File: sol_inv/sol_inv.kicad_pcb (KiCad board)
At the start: 2 copper layers, 0 parts

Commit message: initial component placement
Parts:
- added C1: 1nF, Capacitor_SMD:C_0603_1608Metric, F.Cu at (217.0, 65.0)
- added C10: 10uF, Capacitor_SMD:C_0603_1608Metric, F.Cu at (183.5, 83.5)
- added C11: 10uF, Capacitor_SMD:C_0603_1608Metric, F.Cu at (183.5, 104.5)
- added C12: 10uF, Capacitor_SMD:C_0603_1608Metric, F.Cu at (188.5, 83.3)
- added C13: 0.1uF, Capacitor_SMD:C_0201_0603Metric, F.Cu at (179.3, 92.5)
- added C14: 0.1uF, Capacitor_SMD:C_0201_0603Metric, F.Cu at (184.0, 86.0)
- added C15: 0.1uF, Capacitor_SMD:C_0201_0603Metric, F.Cu at (189.0, 86.0)
- added C16: 0.1uF, Capacitor_SMD:C_0201_0603Metric, F.Cu at (179.3, 98.0)
- added C17: 0.1uF, Capacitor_SMD:C_0201_0603Metric, F.Cu at (191.0, 102.5)
- added C18: 0.1uF, Capacitor_SMD:C_0201_0603Metric, F.Cu at (167.5, 52.8)
- added C19: 0.22uF, Capacitor_SMD:C_0402_1005Metric, F.Cu at (190.0, 86.0)
- added C2: 1nF, Capacitor_SMD:C_0603_1608Metric, F.Cu at (139.8, 109.0)
- added C20: 4.7uF, Capacitor_SMD:C_0402_1005Metric, F.Cu at (179.0, 94.0)
- added C21: 0.1uF, Capacitor_SMD:C_0201_0603Metric, F.Cu at (119.2, 152.5)
- added C22: 0.1uF, Capacitor_SMD:C_0201_0603Metric, F.Cu at (202.0, 46.2)
- added C23: 0.1uF, Capacitor_SMD:C_0201_0603Metric, F.Cu at (119.7, 178.0)
- added C24: 22pF, Capacitor_SMD:C_0805_2012Metric, F.Cu at (162.2, 96.4)
- added C25: 8pF, Capacitor_SMD:C_0402_1005Metric, F.Cu at (173.7, 100.3)
- added C26: 22pF, Capacitor_SMD:C_0805_2012Metric, F.Cu at (162.2, 102.9)
- added C27: 8pF, Capacitor_SMD:C_0402_1005Metric, F.Cu at (171.2, 95.8)
- added C28: 2200uF, Capacitor_THT:CP_Radial_D10.0mm_P5.00mm, F.Cu at (128.3, 62.5)
- added C29: 22uF, Capacitor_SMD:C_1206_3216Metric, F.Cu at (144.8, 59.0)
- added C3: 100uF, Capacitor_SMD:CP_Elec_8x10, F.Cu at (224.2, 74.0)
- added C4: 100uF, Capacitor_SMD:CP_Elec_8x10, F.Cu at (129.5, 110.8)
- added C5: 47uF, Capacitor_SMD:CP_Elec_8x10, F.Cu at (243.5, 92.5)
- added C6: 47uF, Capacitor_SMD:CP_Elec_8x10, F.Cu at (243.2, 82.0)
- added C7: 47uF, Capacitor_SMD:CP_Elec_8x10, F.Cu at (165.5, 130.8)
- added C8: 47uF, Capacitor_SMD:CP_Elec_8x10, F.Cu at (176.0, 130.8)
- added C9: 10uF, Capacitor_SMD:C_0603_1608Metric, F.Cu at (176.7, 93.0)
- added D1: LED, LED_SMD:LED_0603_1608Metric, F.Cu at (187.0, 36.1)
- added D2: LED, LED_SMD:LED_0603_1608Metric, F.Cu at (184.1, 36.1)
- added D3: LED, LED_SMD:LED_0603_1608Metric, F.Cu at (181.0, 36.2)
- added D4: MDB6S, MDB6S:BR_Micro-DIP4_OSI, F.Cu at (114.4, 60.0)
- added F1: MC000827, MC000827:FUSE_MC000827_MTC, F.Cu at (120.8, 30.1)
- added J1: Screw_Terminal_01x02, Wurth-WR-TBL Series:691216610002_Handsolder, F.Cu at (138.5, 92.9)
- added J10: Conn_01x05, Connector_PinSocket_2.54mm:PinSocket_1x05_P2.54mm_Vertical, F.Cu at (217.0, 25.5)
- added J11: IEC_60320_C8_Receptacle, IEC C8 4300-0103:43000103, F.Cu at (62.8, 38.8)
- added J2: Screw_Terminal_01x02, Wurth-WR-TBL Series:691216610002_Handsolder, F.Cu at (198.5, 155.0)
- added J3: Conn_01x06, Connector_PinHeader_2.54mm:PinHeader_1x06_P2.54mm_Vertical, F.Cu at (108.0, 141.1)
- added J4: Conn_01x05, Connector_PinSocket_2.54mm:PinSocket_1x05_P2.54mm_Vertical, F.Cu at (203.1, 25.5)
- added J5: Conn_ARM_JTAG_SWD_10, Connector_PinHeader_1.27mm:PinHeader_2x05_P1.27mm_Vertical, F.Cu at (116.9, 149.8)
- added J6: Conn_01x02, Connector_PinSocket_2.54mm:PinSocket_1x02_P2.54mm_Vertical, F.Cu at (262.0, 49.5)
- added J7: Conn_01x08, Connector_PinSocket_2.54mm:PinSocket_1x08_P2.54mm_Vertical, F.Cu at (163.1, 25.5)
- added J8: Conn_01x08, Connector_PinSocket_2.54mm:PinSocket_1x08_P2.54mm_Vertical, F.Cu at (262.0, 24.8)
- added J9: Conn_01x05, Connector_PinSocket_2.54mm:PinSocket_1x05_P2.54mm_Vertical, F.Cu at (245.2, 25.5)
- added R1: 1kR, Resistor_SMD:R_0805_2012Metric, F.Cu at (199.0, 126.0)
- added R10: 10kR, Resistor_SMD:R_2512_6332Metric, F.Cu at (200.0, 61.5)
- added R11: 10kR, Resistor_SMD:R_2512_6332Metric, F.Cu at (152.5, 76.5)
- added R12: 330R, Resistor_SMD:R_0603_1608Metric, F.Cu at (219.0, 65.0)
- added R13: 330R, Resistor_SMD:R_0603_1608Metric, F.Cu at (139.8, 107.0)
- added R14: 0.01R, WSLP2512R0100FEA:RES_VISHAY_WSLP2512_C_VIS, F.Cu at (249.5, 124.5)
- added R15: 8kR, Resistor_SMD:R_0603_1608Metric, F.Cu at (218.2, 108.2)
- added R16: 1R, Resistor_SMD:R_2010_5025Metric, F.Cu at (186.0, 79.0)
- added R17: 4k7R, Resistor_SMD:R_0402_1005Metric, F.Cu at (170.0, 58.5)
- added R18: 1kR, Resistor_SMD:R_0805_2012Metric, F.Cu at (112.5, 153.1)
- added R19: 1kR, Resistor_SMD:R_0805_2012Metric, F.Cu at (103.5, 149.1)
- added R2: 120kR, Resistor_SMD:R_0805_2012Metric, F.Cu at (185.0, 128.0)
- added R20: 1kR, Resistor_SMD:R_0805_2012Metric, F.Cu at (103.5, 145.6)
- added R21: 1kR, Resistor_SMD:R_0805_2012Metric, F.Cu at (112.5, 142.2)
- added R22: 20R, Resistor_SMD:R_1206_3216Metric, F.Cu at (118.0, 142.5)
- added R23: 330R, Resistor_SMD:R_0603_1608Metric, F.Cu at (187.0, 32.4)
- added R24: 330R, Resistor_SMD:R_0603_1608Metric, F.Cu at (184.1, 32.4)
- added R25: 330R, Resistor_SMD:R_0603_1608Metric, F.Cu at (181.0, 32.6)
- added R26: 4k7R, Resistor_SMD:R_0402_1005Metric, F.Cu at (203.5, 46.2)
- added R27: 4k7R, Resistor_SMD:R_0402_1005Metric, F.Cu at (121.7, 178.0)
- added R28: 120kR, Resistor_SMD:R_0805_2012Metric, F.Cu at (131.0, 98.0)
- added R29: 10kR, Resistor_SMD:R_2512_6332Metric, F.Cu at (126.0, 101.0)
- added R3: 10kR, Resistor_SMD:R_2512_6332Metric, F.Cu at (179.0, 122.5)
- added R4: 120kR, Resistor_SMD:R_0805_2012Metric, F.Cu at (241.0, 100.5)
- added R5: 10kR, Resistor_SMD:R_2512_6332Metric, F.Cu at (236.0, 95.5)
- added R6: 240kR, Resistor_SMD:R_0603_1608Metric, F.Cu at (203.5, 130.5)
- added R7: 240kR, Resistor_SMD:R_0603_1608Metric, F.Cu at (193.5, 130.2)
- added R8: 10kR, Resistor_SMD:R_2512_6332Metric, F.Cu at (200.0, 55.5)
- added R9: 10kR, Resistor_SMD:R_2512_6332Metric, F.Cu at (158.5, 76.6)
- added SW1: SW_Push_Dual, B3F-1000:SW_B3F-1000_OMR, F.Cu at (176.5, 55.0)
- added SW2: SW_Push_Dual, B3F-1000:SW_B3F-1000_OMR, F.Cu at (199.7, 39.1)
- added SW3: SW_Push_Dual, B3F-1000:SW_B3F-1000_OMR, F.Cu at (117.2, 171.0)
- added T1: 12uH, 1.7A, Eagle_WE-FLEX (rev24a):WE-FLEX_EFD20, F.Cu at (261.4, 87.4)
- added T2: 12uH, 1.7A, Eagle_WE-FLEX (rev24a):WE-FLEX_EFD20, F.Cu at (170.1, 149.0)
- added T3: 12uH, 1.7A, Eagle_WE-FLEX (rev24a):WE-FLEX_EFD20, F.Cu at (225.5, 139.5)
- added T4: Transformer_1P_1S, Myrra_44229:44230_MYR, F.Cu at (76.8, 32.6)
- added U1: MCP6001-OT, Package_TO_SOT_SMD:SOT-23-5, F.Cu at (185.4, 123.4)
- added U10: AZ1117CR2-3.3, Package_TO_SOT_SMD:SOT-89-3, F.Cu at (139.8, 60.0)
- added U11: MCP6001-OT, Package_TO_SOT_SMD:SOT-23-5, F.Cu at (128.9, 92.6)
- added U2: MCP6001-OT, Package_TO_SOT_SMD:SOT-23-5, F.Cu at (234.9, 101.5)
- added U3: INA240A1D, INA240A1D:D8_TEX, F.Cu at (199.5, 118.5)
- added U4: INA240A1D, INA240A1D:D8_TEX, F.Cu at (243.5, 117.0)
- added U5: IFX007T, TO127P1500X440-8N-1-V:TO127P1500X440-8N-1-V, F.Cu at (237.4, 62.8)
- added U6: IFX007T, TO127P1500X440-8N-1-V:TO127P1500X440-8N-1-V, F.Cu at (141.7, 123.4)
- added U7: LM4040DIM3-2.5, Package_TO_SOT_SMD:SOT-23-3, F.Cu at (215.6, 100.6)
- added U8: MCP6001-OT, Package_TO_SOT_SMD:SOT-23-5, F.Cu at (213.6, 104.4)
- added U9: PSC3M5_E-LQFP-64, LQFP50P1200X1200X160-65N:LQFP50P1200X1200X160-65N, F.Cu at (187.8, 94.2)
- added Y1: 16MHz, ABLS-16-000MHZ-B2-T:XTAL_ABLS-16_ABR, F.Cu at (166.2, 99.5)
- added Y2: 32.786KHz, LFXTAL002995:XTAL_LFXTAL002995BULK_IQD, F.Cu at (172.2, 98.8)
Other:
- copper layers 2 -> 4
- rule pad_to_mask_clearance: 0 -> 0.05

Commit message: v0.3 pcb layout pre-drc fixes
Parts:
- added C30: 0.1uF, Capacitor_SMD:C_0402_1005Metric, F.Cu at (130.8, 64.5)
- added C31: 0.1uF, Capacitor_SMD:C_0402_1005Metric, F.Cu at (140.2, 64.8)
- C13, C14, C15, C16, C17, C18, C21, C22, C23: footprint Capacitor_SMD:C_0201_0603Metric -> Capacitor_SMD:C_0402_1005Metric
- R10, R11, R29, R3, R5, R8, R9: footprint Resistor_SMD:R_2512_6332Metric -> Resistor_SMD:R_0402_1005Metric
- R14: footprint WSLP2512R0100FEA:RES_VISHAY_WSLP2512_C_VIS -> Resistor_SMD:R_2512_6332Metric
- R16: footprint Resistor_SMD:R_2010_5025Metric -> Resistor_SMD:R_0603_1608Metric
- Y1: footprint ABLS-16-000MHZ-B2-T:XTAL_ABLS-16_ABR -> SamacSys_Parts:ABLS7
- moved J2 199.5 mm to (30.2, 47.8), turned to -90 degrees
- moved J11 177.1 mm to (239.4, 52.6), turned to 90 degrees
- moved T3 165.8 mm to (82.5, 55.5), turned to 180 degrees
- moved C6 163.8 mm to (80.1, 96.3), turned to -90 degrees
- moved C5 156.4 mm to (87.3, 84.3), turned to -90 degrees
- moved T1 155.2 mm to (106.4, 94.2), turned to -90 degrees
- moved T4 150.7 mm to (225.3, 58.8), turned to 180 degrees
- moved C8 148.4 mm to (31.6, 96.3), turned to -90 degrees
- moved U5 146.6 mm to (106.6, 128.8), turned to 90 degrees
- moved R14 145.9 mm to (116.6, 64.3), turned to 90 degrees
- moved C3 145.8 mm to (92.5, 136.5), turned to 90 degrees
- moved R12 136.5 mm to (105.3, 140.5), turned to 0 degrees
- moved C7 134.4 mm to (39.3, 84.3), turned to -90 degrees
- moved C1 130.6 mm to (108.6, 137.8), turned to 180 degrees
- moved U4 128.8 mm to (126.0, 64.3), turned to 90 degrees
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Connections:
- J1 pad 1: +24V -> GND
- J1 pad 2: GND -> +24V
- R1 pad 1: Net-(U3-+) -> Net-(U3--)
- R1 pad 2: Net-(U3--) -> Net-(U3-+)
- R6 pad 1: /H-Bridge/V_OUT_{A} -> /H-Bridge/V_OUT_{B}
- R6 pad 2: Net-(U3-+) -> Net-(U3--)
- R7 pad 1: /H-Bridge/V_OUT_{B} -> /H-Bridge/V_OUT_{A}
- R7 pad 2: Net-(U3--) -> Net-(U3-+)
- U3 pad 3: GNDD -> /H-Bridge/V_{REF}
- U3 pad 7: /H-Bridge/V_{REF} -> GNDD
- U4 pad 1: /H-Bridge/IS_OUT_{B} -> /H-Bridge/IS_OUT_{A}
- U4 pad 3: GNDD -> /H-Bridge/V_{REF}
- U4 pad 7: /H-Bridge/V_{REF} -> GNDD
- U4 pad 8: /H-Bridge/IS_OUT_{A} -> /H-Bridge/IS_OUT_{B}
- U9 pad 46: /H-Bridge/VS_{AC} -> /H-Bridge/VS_{C2}
- U9 pad 48: /H-Bridge/VS_{C2} -> /H-Bridge/VS_{AC}
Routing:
- net +3V3: track 0.00 -> 596.0 mm, vias 0 -> 20
- net GND: track 0.00 -> 485.8 mm, vias 0 -> 2
- net +24V: track 0.00 -> 292.0 mm
- net GNDD: track 0.00 -> 265.8 mm, vias 0 -> 45
- net /H-Bridge/V_OUT_{B}: track 0.00 -> 234.2 mm, vias 0 -> 3
- net /H-Bridge/IS_{B}: track 0.00 -> 168.9 mm, vias 0 -> 2
- net /H-Bridge/V_OUT_{A}: track 0.00 -> 159.6 mm
- net Net-(U6-INH): track 0.00 -> 156.7 mm, vias 0 -> 2
- net Net-(U6-IN): track 0.00 -> 152.6 mm, vias 0 -> 2
- net /H-Bridge/V_{SOURCE}: track 0.00 -> 141.1 mm, vias 0 -> 2
- net Net-(U5-IN): track 0.00 -> 123.1 mm, vias 0 -> 2
- net Net-(U5-INH): track 0.00 -> 118.1 mm, vias 0 -> 2
- net /H-Bridge/IS_{A}: track 0.00 -> 108.4 mm, vias 0 -> 4
- net /H-Bridge/V_{REF}: track 0.00 -> 106.4 mm, vias 0 -> 3
- net Net-(J8-Pin_1): track 0.00 -> 103.1 mm, vias 0 -> 1
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- added copper zone on F.Cu, net +3V3
- added copper zone on F.Cu, net /H-Bridge/H_{1-3}OUT
- added copper zone on F.Cu, net /H-Bridge/H_{2-4}OUT
- added copper zone on F.Cu, net /H-Bridge/IS_OUT_{A}
- added copper zone on F.Cu, net /H-Bridge/IS_OUT_{B}
- added copper zone on F.Cu, net /H-Bridge/V_OUT_{A}
- added copper zone on F.Cu, net /H-Bridge/V_OUT_{B}
- added copper zone on In1.Cu, net GND
- added copper zone on F.Cu, net GNDD
- added copper zone on In1.Cu, net GNDD
- added copper zone on F.Cu, net Net-(T3-Pad10)
- added copper zone on F.Cu, net Net-(T3-Pad11)
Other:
- board outline added: 237.5 x 135.5 mm

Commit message: v0.3.1 drc fixes + layout tweaks
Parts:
- added #SYM1: OSHW-Logo2_14.6x12mm_SilkScreen, Symbol:OSHW-Logo2_14.6x12mm_SilkScreen, F.Cu at (218.0, 148.0)
- added #SYM2: ESD-Logo_6.6x6mm_SilkScreen, Symbol:ESD-Logo_6.6x6mm_SilkScreen, F.Cu at (190.8, 92.2)
- added #SYM3: Symbol_HighVoltage_Triangle_8x7mm_Copper, Symbol:Symbol_HighVoltage_Triangle_8x7mm_Copper, F.Cu at (53.2, 64.2)
- Y2: footprint LFXTAL002995:XTAL_LFXTAL002995BULK_IQD -> PCM_Crystal_AKL:Crystal_DS26_D2.0mm_L6.0mm_Vertical
- moved C27 4.12 mm to (156.8, 101.2), turned to -90 degrees
- moved C25 4.04 mm to (156.8, 103.9), turned to 90 degrees
- moved R2 3.00 mm to (127.5, 74.5)
- moved R28 1.85 mm to (125.8, 110.0)
- moved Y2 1.10 mm to (159.2, 103.5), turned to 90 degrees
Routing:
- net /H-Bridge/V_OUT_{A}: track 159.6 -> 129.7 mm
- net +3V3: track 596.0 -> 609.0 mm
- net /MCU Power/~{XRES_{MCU}}: track 98.4 -> 104.6 mm
- net /H-Bridge/V_OUT_{B}: track 234.2 -> 231.2 mm
- net Net-(U1-+): track 13.0 -> 16.0 mm
- net /MCU IO/HIB: track 72.6 -> 75.1 mm
- net Net-(U11-+): track 15.0 -> 17.0 mm
- net /MCU IO/WCO_IN: track 18.6 -> 16.7 mm
- net +24V: track 292.0 -> 290.7 mm
- added copper zone on In2.Cu, net +3V3
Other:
- rule pad_to_mask_clearance: 0.05 -> 0

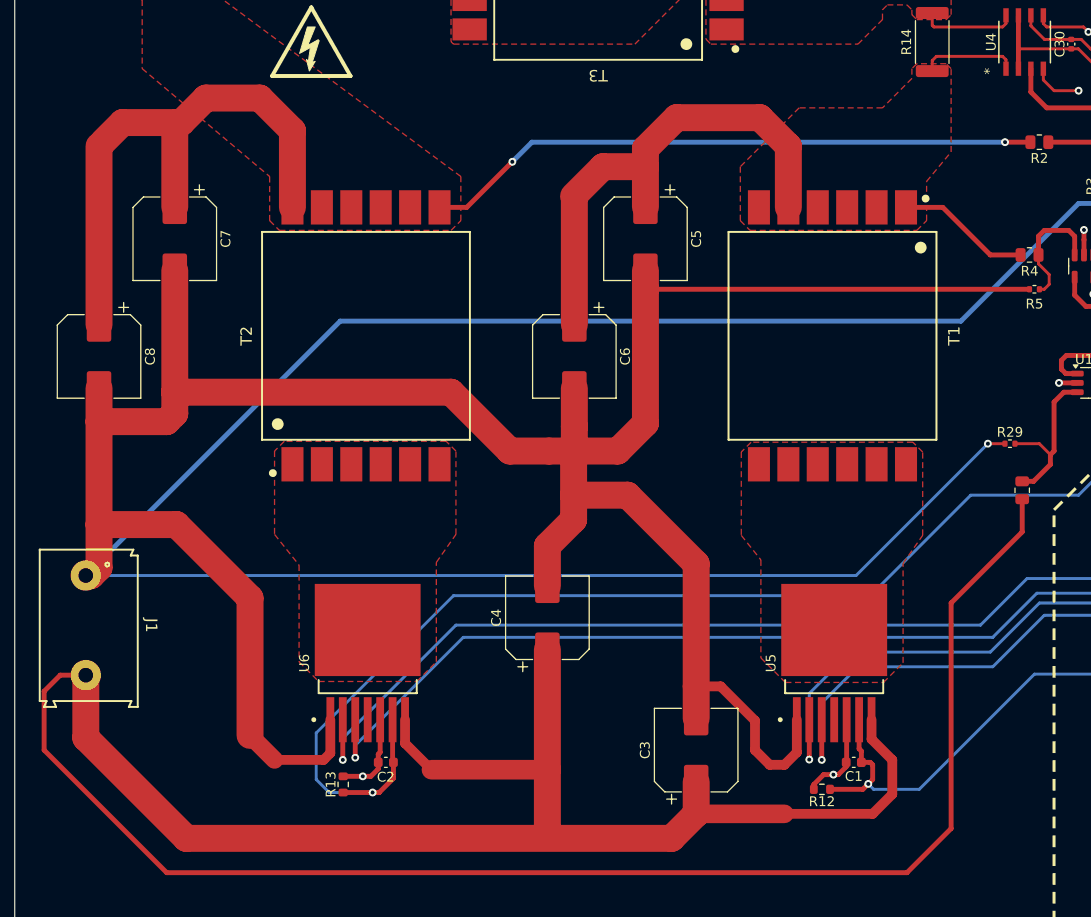
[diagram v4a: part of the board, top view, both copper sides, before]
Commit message: v0.3.2 hbridge plane tweaks
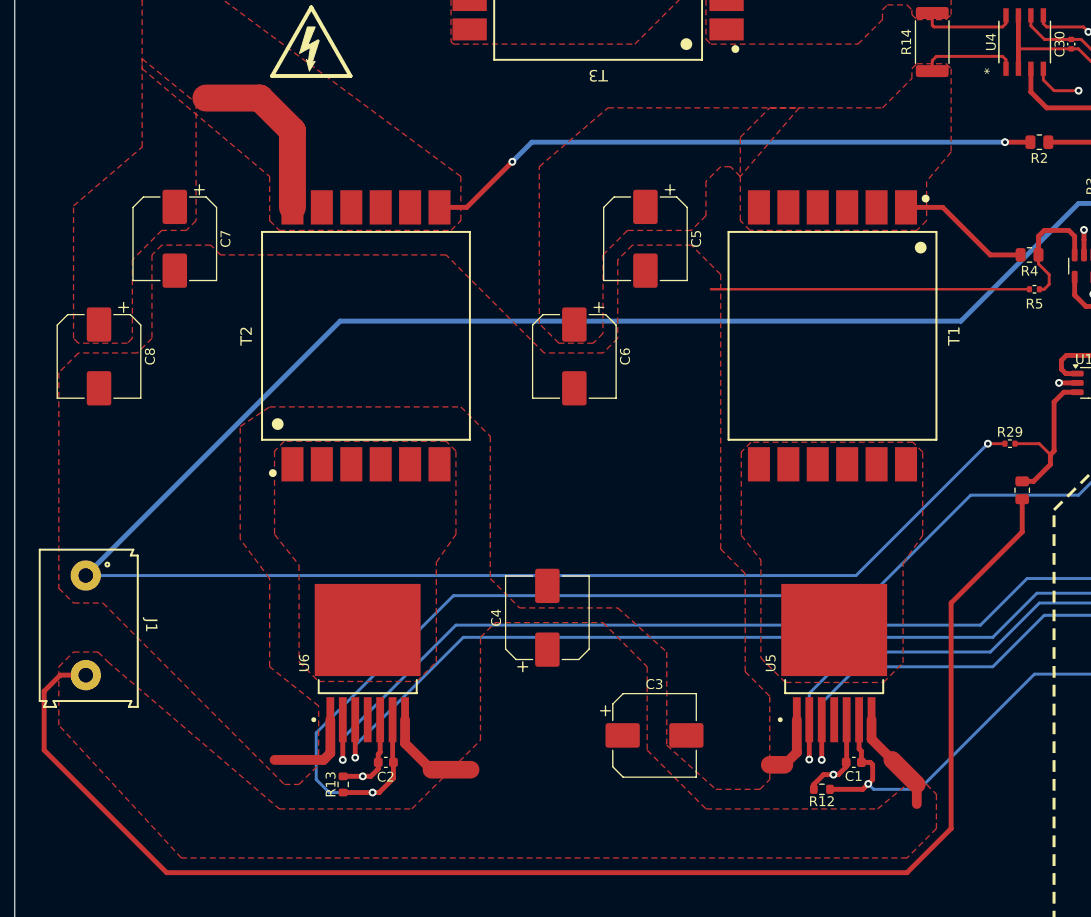
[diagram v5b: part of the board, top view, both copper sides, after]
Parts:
- moved C3 4.51 mm to (88.2, 135.0), turned to 0 degrees
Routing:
- net GND: track 485.8 -> 268.2 mm
- net +24V: track 290.7 -> 167.8 mm
- net /H-Bridge/IS_OUT_{A}: track 74.4 -> 23.5 mm
- net /H-Bridge/V_OUT_{B}: track 231.2 -> 192.0 mm
- added copper zone on F.Cu, net +24V
- added copper zone on F.Cu, net GND
- added copper zone on In2.Cu, net GND

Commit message: v0.3.4 fixes + component change for farnell
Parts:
- added J12: Conn_01x05, Connector_PinSocket_2.54mm:PinSocket_1x05_P2.54mm_Vertical, F.Cu at (212.2, 79.0)
- U3, U4: value INA240A1D -> AD8418; footprint INA240A1D:D8_TEX -> Package_SO:SOIC-8_3.9x4.9mm_P1.27mm
- Y2: footprint PCM_Crystal_AKL:Crystal_DS26_D2.0mm_L6.0mm_Vertical -> Crystal:Crystal_DS26_D2.0mm_L6.0mm_Vertical
- moved R7 18.8 mm to (125.4, 49.7), turned to 0 degrees
- moved R6 12.6 mm to (125.4, 57.2), turned to 0 degrees
- moved R1 12.3 mm to (127.9, 53.7), turned to -90 degrees
- moved C31 11.2 mm to (141.8, 53.7), turned to 90 degrees
- moved U3 7.24 mm to (136.8, 53.7), turned to 90 degrees
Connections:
- R1 pad 1: Net-(U3--) -> Net-(U3-IN+)
- R1 pad 2: Net-(U3-+) -> Net-(U3-IN-)
- R6 pad 2: Net-(U3--) -> Net-(U3-IN-)
- R7 pad 2: Net-(U3-+) -> Net-(U3-IN+)
- U3 pad 1: Net-(U3--) -> Net-(U3-IN-)
- U3 pad 3: /H-Bridge/V_{REF} -> GNDD
- U3 pad 4: GNDD -> unconnected-(U3-NC-Pad4)
- U3 pad 7: GNDD -> /H-Bridge/V_{REF}
- U3 pad 8: Net-(U3-+) -> Net-(U3-IN+)
- U4 pad 3: /H-Bridge/V_{REF} -> GNDD
- U4 pad 4: GNDD -> unconnected-(U4-NC-Pad4)
- U4 pad 7: GNDD -> /H-Bridge/V_{REF}
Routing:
- net /H-Bridge/VS_{AC}: track 70.0 -> 122.4 mm, vias 0 -> 1
- net /H-Bridge/VS_{C1}: track 68.0 -> 105.7 mm
- net /H-Bridge/VS_{C2}: track 70.6 -> 105.5 mm
- net GNDD: track 265.5 -> 230.7 mm, vias 45 -> 42
- net /H-Bridge/IS_{AC}: track 83.4 -> 114.7 mm
- net /H-Bridge/V_OUT_{A}: track 129.7 -> 108.4 mm
- net /H-Bridge/V_OUT_{B}: track 192.0 -> 177.9 mm
- net Net-(U3-IN+): track 0.00 -> 12.7 mm
- net Net-(U3-IN-): track 0.00 -> 12.2 mm
- net /H-Bridge/V_{REF}: track 106.4 -> 118.1 mm, vias 3 -> 4
- net Net-(U3-+): track 9.74 -> 0.00 mm
- net Net-(U3--): track 9.40 -> 0.00 mm
- net +3V3: track 609.0 -> 610.3 mm

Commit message: v0.4 fixed mcu ldo part, production testing
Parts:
- added FID1**: Fiducial_1mm_Mask2mm, Fiducial:Fiducial_1mm_Mask2mm, F.Cu at (34.0, 31.0)
- added FID2**: Fiducial_1mm_Mask2mm, Fiducial:Fiducial_1mm_Mask2mm, F.Cu at (257.0, 30.8)
- added FID3**: Fiducial_1mm_Mask2mm, Fiducial:Fiducial_1mm_Mask2mm, F.Cu at (33.5, 153.5)
- U10: value AZ1117CR2-3.3 -> AZ1117CR-3.3
- moved #SYM1 5.70 mm to (222.5, 151.5)
- moved #SYM2 5.70 mm to (195.2, 95.8)
- moved C11 5.70 mm to (174.5, 118.7)
- moved C13 5.70 mm to (171.5, 106.2)
- moved C16 5.70 mm to (172.5, 113.8)
- moved C17 5.70 mm to (185.5, 116.8)
- moved C18 5.70 mm to (178.0, 134.8)
- moved C19 5.70 mm to (184.2, 97.7)
- moved C20 5.70 mm to (172.0, 107.8)
- moved C21 5.70 mm to (156.8, 147.0)
- moved C22 5.70 mm to (201.7, 150.0)
- moved C23 5.70 mm to (215.5, 136.0)
- moved C24 5.70 mm to (160.6, 117.8)
- moved C26 5.70 mm to (167.1, 117.8)
- moved C29 5.70 mm to (169.2, 75.8)
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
